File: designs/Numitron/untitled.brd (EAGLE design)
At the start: 40 x 86 mm, 10 parts, among them IC2 TLC5916IN, IC3 TLC5916IN, IC4 TLC5916IN, IC5 TLC5916IN

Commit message: added designs Numitron modular first finish review tomorrow or tuesday
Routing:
- net R-EXT: track 0.00 -> 188.0 mm, vias 0 -> 2
- net CLK1: track 0.00 -> 69.3 mm, vias 0 -> 2
- net N$31: track 0.00 -> 41.7 mm
- net N$32: track 0.00 -> 36.8 mm, vias 0 -> 2
- net N$26: track 0.00 -> 36.5 mm
- net N$67: track 0.00 -> 36.1 mm, vias 0 -> 4
- net LE1: track 0.00 -> 35.5 mm
- net N$30: track 0.00 -> 33.2 mm, vias 0 -> 3
- net N$68: track 0.00 -> 33.1 mm
- net LE2: track 0.00 -> 33.0 mm
- net N$25: track 0.00 -> 31.3 mm
- net SDI1: track 0.00 -> 30.2 mm
- net CLK2: track 0.00 -> 29.3 mm
- net N$36: track 0.00 -> 28.0 mm, vias 0 -> 1
- net N$27: track 0.00 -> 27.7 mm
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- added copper zone on layer 1, net GND
- added copper zone on layer 16, net GND

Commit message: added last design tunes
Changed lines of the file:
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@@
 <?xml version="1.0" encoding="utf-8"?>
 <!DOCTYPE eagle SYSTEM "eagle.dtd">
-<eagle version="9.4.2">
+<eagle version="9.5.1">
 <drawing>
 <settings>
-<setting alwaysvectorfont="yes"/>
+<setting alwaysvectorfont="no"/>
 <setting verticaltext="up"/>
 </settings>
@@
 <wire x1="18.246459375" y1="18.3272" x2="10.61405" y2="18.3272" width="0.2" layer="1"/>
 <wire x1="10.61405" y1="18.3272" x2="9.08" y2="16.79315" width="0.2" layer="1"/>
-<via x="24.0468" y="39.967953125" extent="1-16" drill="0.6"/>
-<wire x1="24.0468" y1="39.967953125" x2="10.8" y2="39.967953125" width="0.2" layer="16"/>
+<via x="23.5468" y="39.967953125" extent="1-16" drill="0.6"/>
+<wire x1="23.5468" y1="39.967953125" x2="10.8" y2="39.967953125" width="0.2" layer="16"/>
 <via x="10.8" y="40" extent="1-16" drill="0.6"/>
 <wire x1="10.8" y1="40" x2="4" y2="40" width="0.2" layer="1"/>
 <wire x1="4" y1="40" x2="4" y2="39.19" width="0.2" layer="1"/>
 <wire x1="10.8" y1="39.967953125" x2="10.8" y2="40" width="0.2" layer="16"/>
-<wire x1="25.903203125" y1="39.967953125" x2="24.0468" y2="39.967953125" width="0.2" layer="1"/>
+<wire x1="25.903203125" y1="39.967953125" x2="23.5468" y2="39.967953125" width="0.2" layer="1"/>
 <wire x1="25.903203125" y1="25.98394375" x2="25.903203125" y2="39.967953125" width="0.2" layer="1"/>
 </signal>

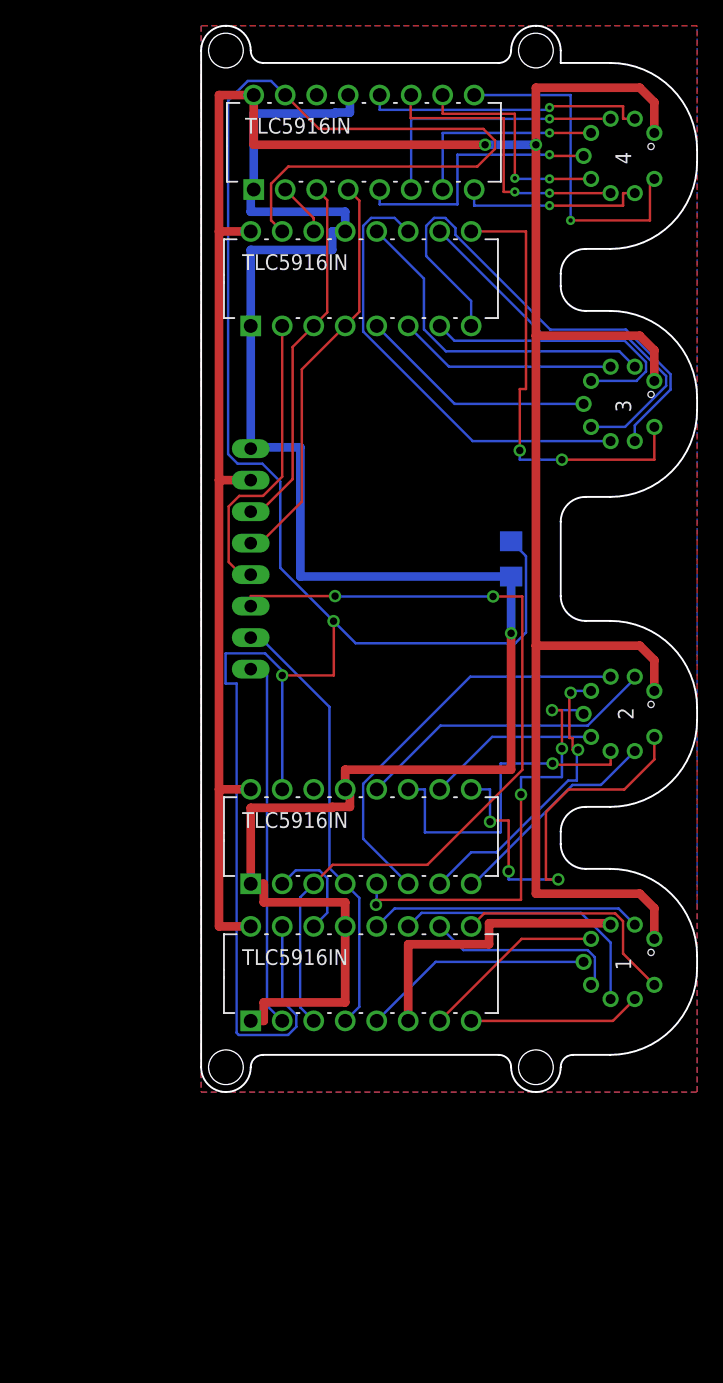
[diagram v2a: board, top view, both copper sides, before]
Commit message: numitron 4 resistor error correction
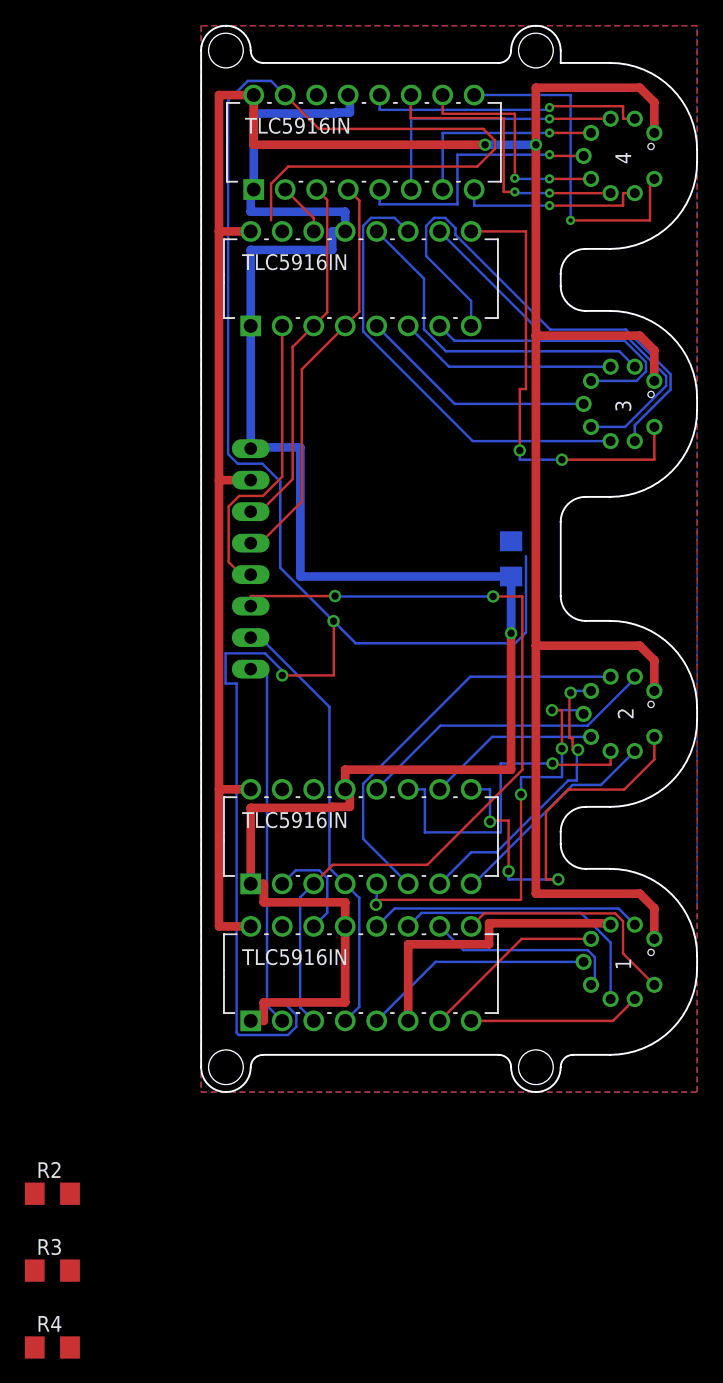
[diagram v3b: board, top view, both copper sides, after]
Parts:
- added R2, R3, R4: 1K, rcl:R1206
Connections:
- removed net R-EXT: IC2.15, IC3.15, IC4.15, IC5.15, R1.2
- new net R-EXT1: IC4.15, R1.2
- new net R-EXT2: IC2.15, R2.2
- new net R-EXT3: IC3.15, R3.2
- new net R-EXT4: IC5.15, R4.2
- net GND: now also R2.1, R3.1, R4.1
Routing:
- net R-EXT: track 188.0 -> 0.00 mm, vias 2 -> 0
- net R-EXT4: track 0.00 -> 169.8 mm, vias 0 -> 2
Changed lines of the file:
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@@
 <?xml version="1.0" encoding="utf-8"?>
 <!DOCTYPE eagle SYSTEM "eagle.dtd">
-<eagle version="9.5.1">
+<eagle version="9.4.2">
 <drawing>
 <settings>
@@
 <attribute name="VALUE" x="1.079" y="41.73" size="1.27" layer="28" ratio="10" rot="MR90"/>
 </element>
+<element name="R2" library="rcl" library_urn="urn:adsk.eagle:library:334" package="R1206" package3d_urn="urn:adsk.eagle:package:23540/2" value="1K" x="-12" y="-8.2" smashed="yes">
+<attribute name="NAME" x="-13.27" y="-6.93" size="1.27" layer="25"/>
+<attribute name="SPICEPREFIX" value="R" x="-12" y="-8.2" size="1.778" layer="27" display="off"/>
+<attribute name="VALUE" x="-13.27" y="-10.74" size="1.27" layer="27"/>
+</element>
+<element name="R3" library="rcl" library_urn="urn:adsk.eagle:library:334" package="R1206" package3d_urn="urn:adsk.eagle:package:23540/2" value="1K" x="-12" y="-14.4" smashed="yes">
+<attribute name="NAME" x="-13.27" y="-13.13" size="1.27" layer="25"/>
+<attribute name="SPICEPREFIX" value="R" x="-12" y="-14.4" size="1.778" layer="27" display="off"/>
+<attribute name="VALUE" x="-13.27" y="-16.94" size="1.27" layer="27"/>
+</element>
+<element name="R4" library="rcl" library_urn="urn:adsk.eagle:library:334" package="R1206" package3d_urn="urn:adsk.eagle:package:23540/2" value="1K" x="-12" y="-20.6" smashed="yes">
+<attribute name="NAME" x="-13.27" y="-19.33" size="1.27" layer="25"/>
+<attribute name="SPICEPREFIX" value="R" x="-12" y="-20.6" size="1.778" layer="27" display="off"/>
+<attribute name="VALUE" x="-13.27" y="-23.14" size="1.27" layer="27"/>
+</element>
 </elements>
 <signals>
@@
 <vertex x="0" y="86"/>
 </polygon>
+<contactref element="R2" pad="1"/>
+<contactref element="R3" pad="1"/>
+<contactref element="R4" pad="1"/>
+<wire x1="-13.422" y1="-14.4" x2="-13.422" y2="-20.6" width="0" layer="19" extent="1-1"/>
+<wire x1="-13.422" y1="-8.2" x2="-13.422" y2="-14.4" width="0" layer="19" extent="1-1"/>
+<wire x1="4" y1="5.74" x2="-13.422" y2="-8.2" width="0" layer="19" extent="1-1"/>
 </signal>
 <signal name="3.3V">
@@
 <wire x1="29.8" y1="70.3" x2="29.8" y2="80.41" width="0.2" layer="16"/>
 </signal>
-<signal name="R-EXT">
-<contactref element="IC4" pad="15"/>
-<contactref element="IC2" pad="15"/>
-<contactref element="IC3" pad="15"/>
+<signal name="R-EXT4">
+<contactref element="R4" pad="2"/>
 <contactref element="IC5" pad="15"/>
-<contactref element="R1" pad="2"/>
 <wire x1="6.78" y1="80.41" x2="9.508434375" y2="77.681565625" width="0.2" layer="1"/>
 <wire x1="9.508434375" y1="77.681565625" x2="22.757540625" y2="77.681565625" width="0.2" layer="1"/>
@@
 <wire x1="7.02454375" y1="74.6442125" x2="5.641796875" y2="73.261465625" width="0.2" layer="1"/>
 <wire x1="5.641796875" y1="73.261465625" x2="5.641796875" y2="70.308203125" width="0.2" layer="1"/>
-<wire x1="5.641796875" y1="70.308203125" x2="6.54" y2="69.41" width="0.2" layer="1"/>
 <wire x1="6.78" y1="80.41" x2="5.641796875" y2="81.548203125" width="0.2" layer="16"/>
 <wire x1="5.641796875" y1="81.548203125" x2="3.768534375" y2="81.548203125" width="0.2" layer="16"/>
@@
 <wire x1="25.332703125" y1="36.196796875" x2="26.201509375" y2="37.065603125" width="0.2" layer="16"/>
 <wire x1="26.201509375" y1="37.065603125" x2="26.201509375" y2="43.220490625" width="0.2" layer="16"/>
-<wire x1="26.201509375" y1="43.220490625" x2="25" y2="44.422" width="0.2" layer="16"/>
 <wire x1="6.54" y1="34.001996875" x2="5.162" y2="35.38" width="0.2" layer="16"/>
 <wire x1="6.54" y1="34.001996875" x2="6.54" y2="33.601996875" width="0.2" layer="16"/>
@@
 <wire x1="7.678203125" y1="5.268534375" x2="7.678203125" y2="6.21146875" width="0.2" layer="16"/>
 <wire x1="7.678203125" y1="6.21146875" x2="6.54" y2="7.349671875" width="0.2" layer="16"/>
-<wire x1="6.54" y1="7.349671875" x2="6.54" y2="13.36" width="0.2" layer="16"/>
 <via x="6.54" y="33.601996875" extent="1-16" drill="0.6"/>
-<wire x1="6.54" y1="24.41315" x2="6.54" y2="33.601996875" width="0.2" layer="16"/>
 <wire x1="6.54" y1="33.601996875" x2="10.7" y2="33.601996875" width="0.2" layer="1"/>
 <wire x1="10.7" y1="33.601996875" x2="10.7" y2="38" width="0.2" layer="1"/>
@@
 <wire x1="1.9728" y1="35.38" x2="5.162" y2="35.38" width="0.2" layer="16"/>
 <wire x1="2.861790625" y1="4.777525" x2="2.861790625" y2="32.9464" width="0.2" layer="16"/>
+<wire x1="3.037525" y1="4.601790625" x2="-10.578" y2="-20.6" width="0" layer="19" extent="1-16"/>
+</signal>
+<signal name="R-EXT3">
+<contactref element="R3" pad="2"/>
+<contactref element="IC3" pad="15"/>
+<wire x1="-10.578" y1="-14.4" x2="6.54" y2="69.41" width="0" layer="19" extent="1-1"/>
+</signal>
+<signal name="R-EXT2">
+<contactref element="R2" pad="2"/>
+<contactref element="IC2" pad="15"/>
+<wire x1="-10.578" y1="-8.2" x2="6.54" y2="24.41315" width="0" layer="19" extent="1-1"/>
+</signal>
+<signal name="R-EXT1">
+<contactref element="R1" pad="2"/>
+<contactref element="IC4" pad="15"/>
+<wire x1="6.54" y1="13.36" x2="25" y2="44.422" width="0" layer="19" extent="16-16"/>
 </signal>
 </signals>

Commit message: corrected numitron pcb
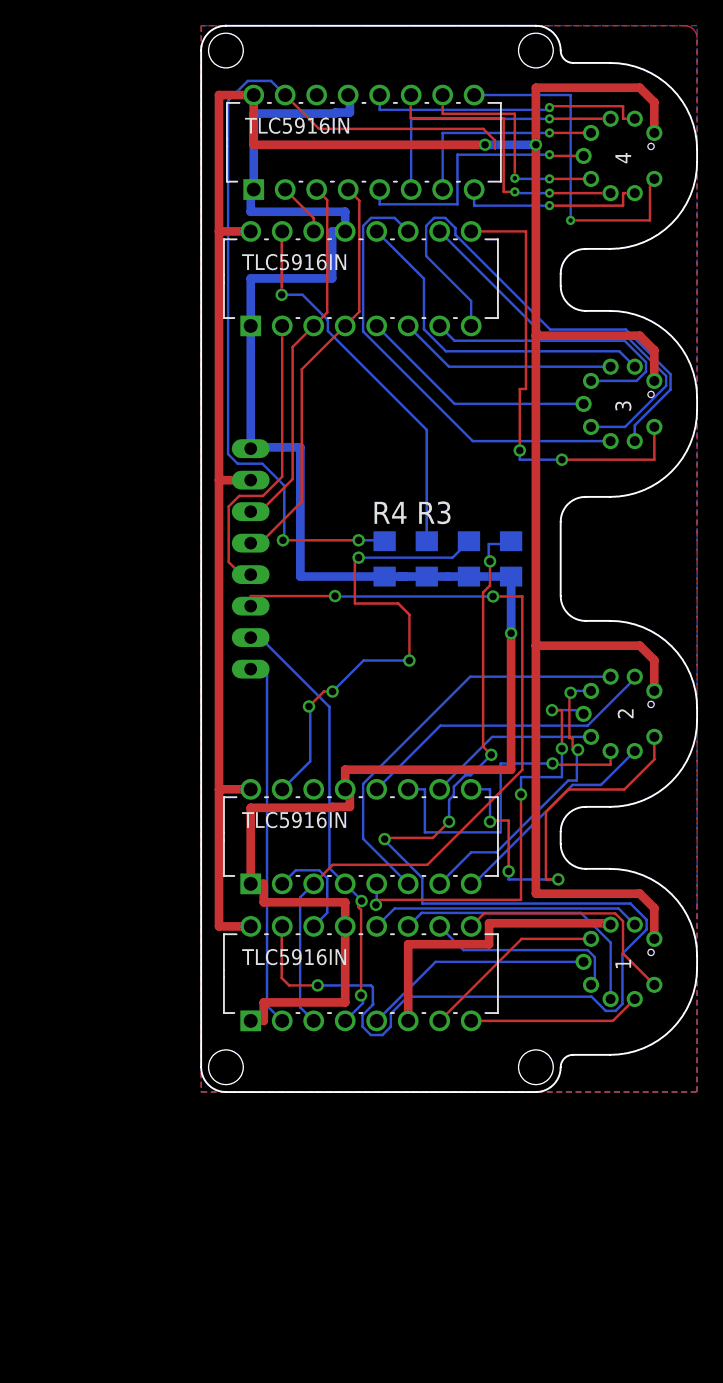
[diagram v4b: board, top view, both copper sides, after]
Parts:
- moved R4 69.0 mm to (14.8, 43.0), flipped to the bottom, turned to 90 degrees
- moved R3 64.9 mm to (18.2, 43.0), flipped to the bottom, turned to 90 degrees
- moved R2 61.2 mm to (21.6, 43.0), flipped to the bottom, turned to 90 degrees
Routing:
- net R-EXT1: track 0.00 -> 104.3 mm, vias 0 -> 5
- net R-EXT4: track 169.8 -> 72.3 mm
- net R-EXT2: track 0.00 -> 39.0 mm, vias 0 -> 4
- net R-EXT3: track 0.00 -> 30.8 mm, vias 0 -> 1
- net GND: track 156.3 -> 161.0 mm
- net LE1: track 35.5 -> 36.1 mm, vias 0 -> 2
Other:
- outline, holes or cut-outs redrawn
